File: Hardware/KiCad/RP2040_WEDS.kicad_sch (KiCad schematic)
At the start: 71 parts, among them J1 Barrel_Jack_Switch_Pin3Ring, J2 Conn_01x02_Male, J3 I2C Soil Header, J4 LiPo Batt, J5 Analog Soil Header, J6 USB Header, J7 Conn_02x05_Odd_Even, J8 SMA-J-P-H-RA-TH1, J9 Solar, Q1 Q_PMOS_DGS, Q2 Q_PMOS_DGS, SW1 SW_Push, SW2 SW_Push, SW3 SW_Push, U1 RP2040, U2 MCP73831-2-OT, U3 W25Q128JVS, U4 BME280, U5 XC6210B332MR, U6 LoRa-E5, U7 TPL5110, Y1 Crystal_GND24

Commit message: Version 1.2 board
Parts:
- removed J1: Barrel_Jack_Switch_Pin3Ring, 54-00125:54-00125, symbol Connector:Barrel_Jack_Switch_Pin3Ring
- added D4: LED, LED_SMD:LED_0603_1608Metric, symbol Device:LED
- added R10, R18, R19, R2, R20, R21: 0, Resistor_SMD:R_0603_1608Metric, symbol Device:R
- added R22: 470, Resistor_SMD:R_0603_1608Metric, symbol Device:R
- added TP4: GND, TestPoint:TestPoint_Loop_D1.80mm_Drill1.0mm_Beaded, symbol Connector:TestPoint
- added TP5: 1V1, TestPoint:TestPoint_Loop_D1.80mm_Drill1.0mm_Beaded, symbol Connector:TestPoint
- added TP8: Q1, TestPoint:TestPoint_Loop_D1.80mm_Drill1.0mm_Beaded, symbol Connector:TestPoint
- J2: value Conn_01x02_Male -> USB BOOT
- J7: value Conn_02x05_Odd_Even -> SWD Header
- J8: value SMA-J-P-H-RA-TH1 -> SMA-Conn
- J9: value Solar -> Solar Panel Input
- JP1: value SolderJumper_2_Open -> Power Isolation
- R11, R12: value 10k -> 4.7k
- TP1: value TestPoint -> 3V3
- TP2: value TestPoint -> VDD
- TP3: value TestPoint -> VDC
- TP6: value TestPoint -> LoRa_TX
- TP7: value TestPoint -> LoRa_RX
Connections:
- net +1V1: now also TP5.1
- net +3V3: now also R21.1; no longer U5.5 (VOUT)
- net +BATT: now also R2.1; no longer U2.3 (VBAT)
- net GND: now also C9.1, R5.2, R22.2, TP4.1; no longer C9.2
- net RESET: no longer U6.17 (RST)
- net VDC: now also D4.2 (A), R10.1, R20.1; no longer D2.2 (A), J6.1 (Pin_1), J9.1 (Pin_1), U2.4 (VDD)
- net VDD: now also C9.2, R18.1, R19.1; no longer C9.1, J3.1 (Pin_1), J5.1 (Pin_1)
- net at D1.2 (A): now also J9.1 (Pin_1)
- net at U2.1 (STAT): now also D2.2 (A); no longer R5.2
- net at C14.1, D3.1 (K), Q1.3 (S)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: now also TP8.1
- net NRST: now reaches U1.4 (GPIO2)
- net NRST: now also U6.17 (RST)
- new net: R2.2, U2.3 (VBAT)
- new net: R10.2, U2.4 (VDD)
- new net: J5.1 (Pin_1), R19.2
- new net: J3.1 (Pin_1), R18.2
- new net: D4.1 (K), R22.1
- new net: R21.2, U5.5 (VOUT)
- new net: J6.1 (Pin_1), R20.2
- no-connect marks 43 -> 42
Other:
- note added: "Full"
- note added: "Power"
- moved on the sheet: C11, C16, C18, C19, C2, C20, C21, C22, C23, C24, C3, C4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

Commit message: v1.2
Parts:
- R7: value 10k -> DNP
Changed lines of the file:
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@@
   (symbol (lib_id "Device:R") (at 224.79 140.97 180) (unit 1)
     (in_bom yes) (on_board yes)
-    (property "Reference" "R7" (id 0) (at 227.33 139.7 0))
-    (property "Value" "10k" (id 1) (at 227.33 142.24 0))
+    (property "Reference" "R7" (id 0) (at 228.6 139.7 0))
+    (property "Value" "DNP" (id 1) (at 228.6 142.24 0))
     (property "Footprint" "Resistor_SMD:R_0603_1608Metric" (id 2) (at 226.568 140.97 90)
       (effects (font (size 1.27 1.27)) hide)
@@
     )
     (path "/00000000-0000-0000-0000-000062196411"
-      (reference "R7") (unit 1) (value "10k") (footprint "Resistor_SMD:R_0603_1608Metric")
+      (reference "R7") (unit 1) (value "DNP") (footprint "Resistor_SMD:R_0603_1608Metric")
     )
     (path "/00000000-0000-0000-0000-00006244e284"

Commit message: v1.2
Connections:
- net D+: no longer names the net of R4.1, U1.47 (USB_DP)
- net D-: no longer names the net of R3.1, U1.46 (USB_DM)
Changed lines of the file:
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@@
-    (effects (font (size 1.27 1.27)) (justify left bottom))
-  )
-  (label "D-" (at 83.82 111.76 0)
     (effects (font (size 1.27 1.27)) (justify left bottom))
   )
@@
     (effects (font (size 1.27 1.27)) (justify left bottom))
   )
-  (label "D+" (at 83.82 114.3 0)
-    (effects (font (size 1.27 1.27)) (justify left bottom))
-  )

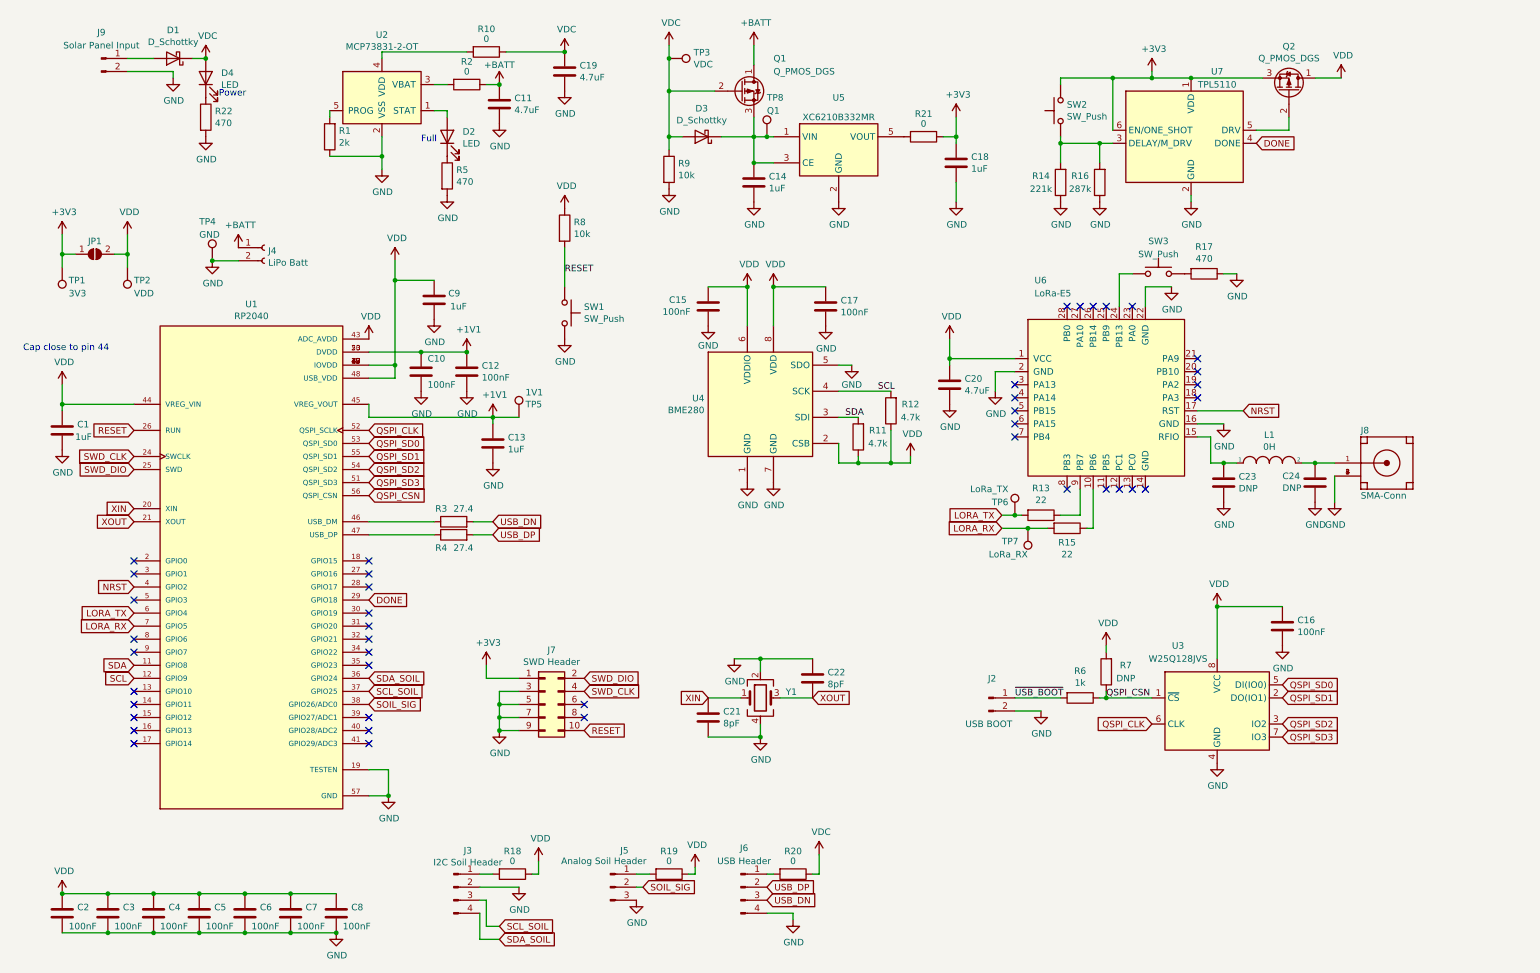
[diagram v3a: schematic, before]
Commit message: added lables and boxes to schematic
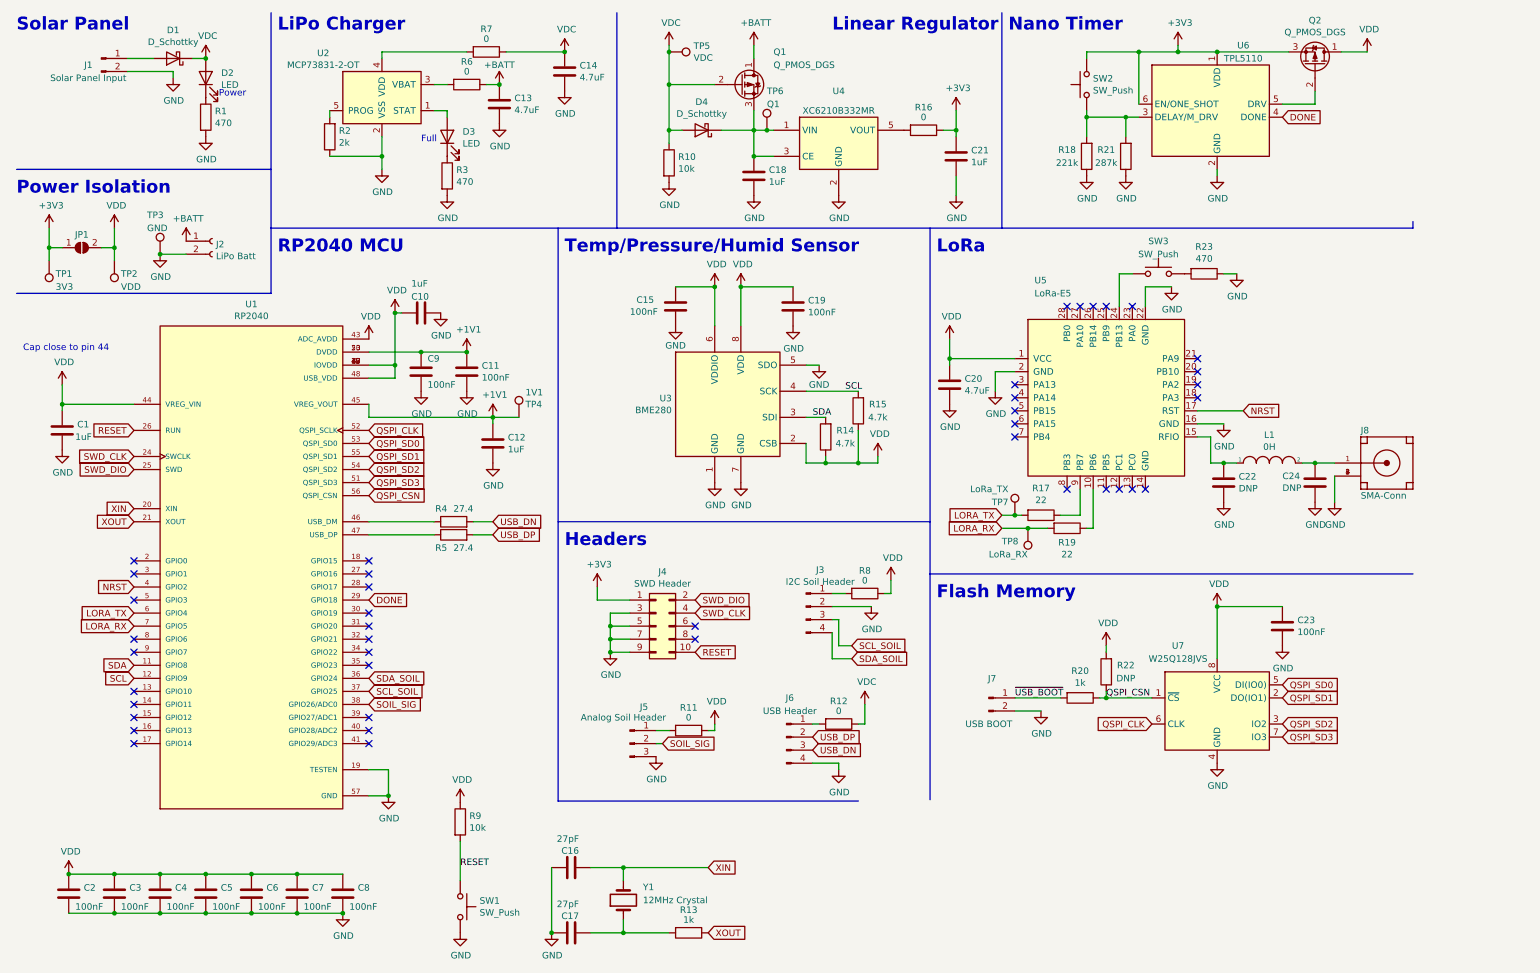
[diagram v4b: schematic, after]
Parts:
- removed C21, C22: 8pF, Capacitor_SMD:C_0603_1608Metric, symbol Device:C
- removed Y1: Crystal_GND24, Oscillator:Oscillator_SMD_Abracon_ASDMB-4Pin_2.5x2.0mm, symbol Device:Crystal_GND24
- added C16, C17: 27pF, Capacitor_SMD:C_0603_1608Metric, symbol Device:C
- added R13: 1k, Resistor_SMD:R_0603_1608Metric, symbol Device:R
- added Y1: 12MHz Crystal, 54-00125:XTAL1140X470X420N, symbol Device:Crystal
- J4: renamed from J7; footprint Connector_PinHeader_1.27mm:PinHeader_2x05_P1.27mm_Vertical_SMD -> Connector_PinHeader_1.27mm:PinHeader_2x05_P1.27mm_Vertical
- U2: MANUFACTURER (none) -> Microchip
- U3: renamed from U4; MANUFACTURER (none) -> Bosch
- U4: renamed from U5; MANUFACTURER (none) -> Torex
- U5: renamed from U6; MANUFACTURER (none) -> Seeed
- U6: renamed from U7; MANUFACTURER (none) -> Texas Instruments
- U7: renamed from U3; MANUFACTURER (none) -> Winbond
- renumbered C9 to C10, C12 to C11, C13 to C12, C11 to C13, C19 to C14, C14 to C18, C17 to C19, C18 to C21, C23 to C22, C16 to C23, C10 to C9, D4 to D2, D2 to D3, D3 to D4, J9 to J1, J4 to J2, J2 to J7, R22 to R1, R9 to R10, R19 to R11, R20 to R12, R11 to R14, R12 to R15, R21 to R16, R13 to R17, R14 to R18, R15 to R19, R1 to R2, R6 to R20, R16 to R21, R7 to R22, R17 to R23, R5 to R3, R3 to R4, R4 to R5, R2 to R6, R10 to R7, R18 to R8, R8 to R9, TP4 to TP3, TP5 to TP4, TP3 to TP5, TP8 to TP6, TP6 to TP7, TP7 to TP8
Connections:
- net GND: now also C16.1, C17.1
- net XIN: now also C16.2, Y1.2
- net XOUT: now also R13.1
- new net: C17.2, R13.2, Y1.1
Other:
- note added: "Flash Memory"
- note added: "Headers"
- note added: "LiPo Charger"
- note added: "Linear Regulator"
- note added: "LoRa"
- note added: "Nano Timer"
- note added: "Power Isolation"
- note added: "RP2040 MCU"
- note added: "Solar Panel"
- note added: "Temp/Pressure/Humid Sensor"
- company: (none) -> Western Washington University
- title: (none) -> WildEDS (Wildfire Early Detection System)
- moved on the sheet: C10, C15, C18, C19, C2, C21, C3, C4, C5, C6, C7, C8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
